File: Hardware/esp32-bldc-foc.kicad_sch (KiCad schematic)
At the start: 51 parts, among them J1 USB_C_Receptacle_USB2.0_14P, J2 Conn_01x03, J3 Conn_01x03, J4 Conn_01x02_Pin, J6 Conn_01x03, Q1 AP30H80Q, SW1 SW_Push_Dual, U1 ESP32-S3-WROOM-1, U2 SRV05-4, U3 MP1584EN-LF-P, U4 AMS1117, U5 EG2133, U6 INA181A1IDBVR

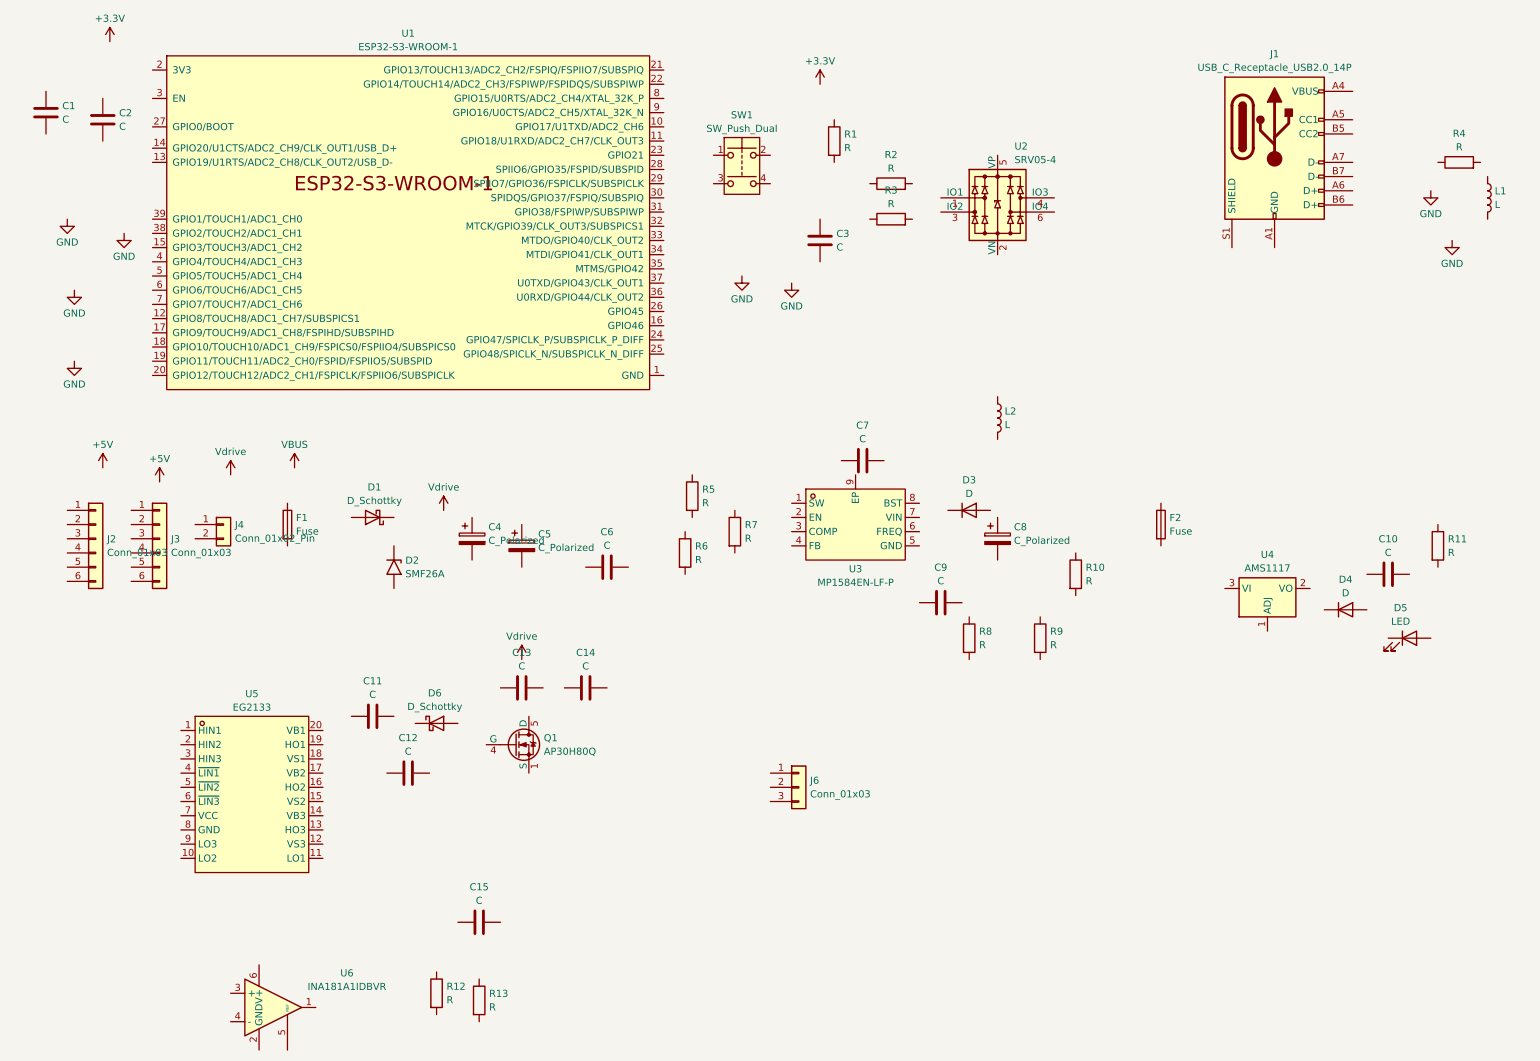
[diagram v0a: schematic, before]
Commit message: First cut of power regulation wiring
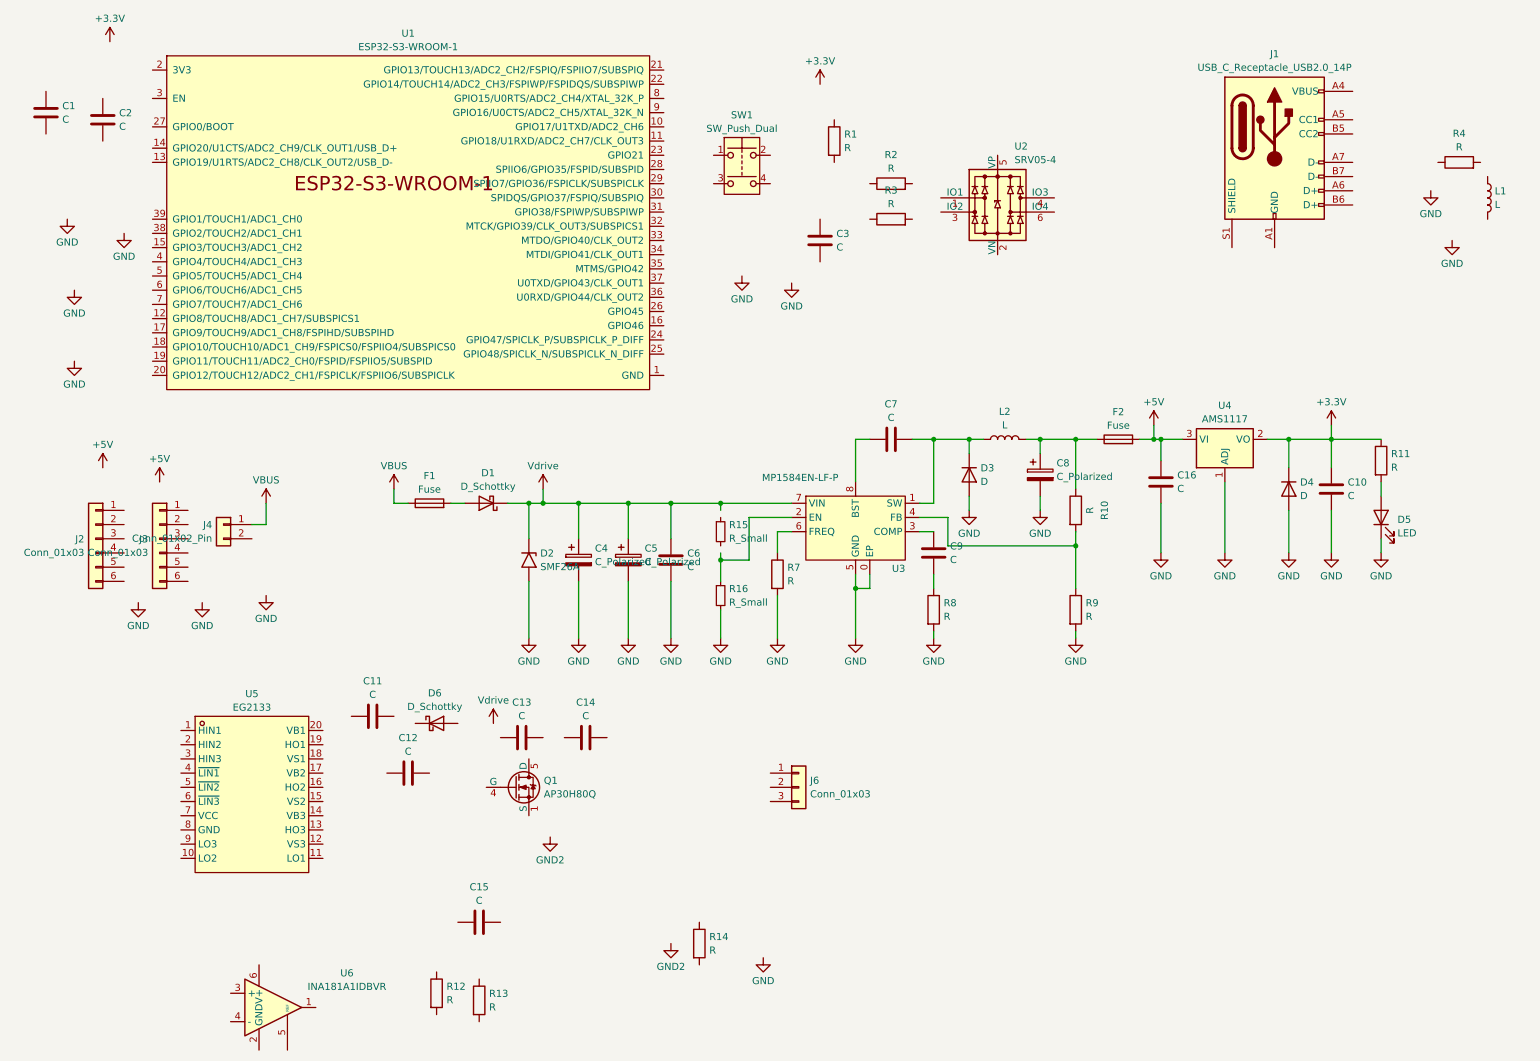
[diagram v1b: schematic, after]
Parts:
- removed R5, R6: R, symbol Device:R
- added C16: C, symbol Device:C
- added R14: R, symbol Device:R
- added R15, R16: R_Small, symbol Device:R_Small
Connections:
- net +3.3V: now also C10.2, D4.1 (K), R11.1, U4.2 (VO)
- net +5V: now also F2.2, U4.3 (VI), C16.2
- net GND: now also C10.1, C4.2, C5.2, C6.1, C8.2, D2.2 (A2), D3.2 (A), D4.2 (A), D5.1 (K), R7.2, R8.2, R9.2, U3.0 (EP), U3.5 (GND), U4.1 (ADJ), C16.1, R16.2
- net VBUS: now also F1.1, J4.1 (Pin_1)
- net Vdrive: now also C4.1, C5.1, C6.2, D1.1 (K), D2.1 (A1), U3.7 (VIN)
- net at R7.1: now also U3.6 (FREQ)
- net at R8.1: now also C9.1
- net at D1.2 (A): now also F1.2
- net at D5.2 (A): now also R11.2
- net at C8.1: now also F2.1, L2.2, R10.1
- net at C7.1: now also U3.8 (BST)
- net at C7.2: now also D3.1 (K), L2.1, U3.1 (SW)
- net at U3.2 (EN): now also R16.1
- net at U3.3 (COMP): now also C9.2
- net at U3.4 (FB): now also R10.2, R9.1
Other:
- moved on the sheet: C10, C13, C14, C4, C5, C6, C7, C8, C9, D1, D2, D3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

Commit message: Placed all components
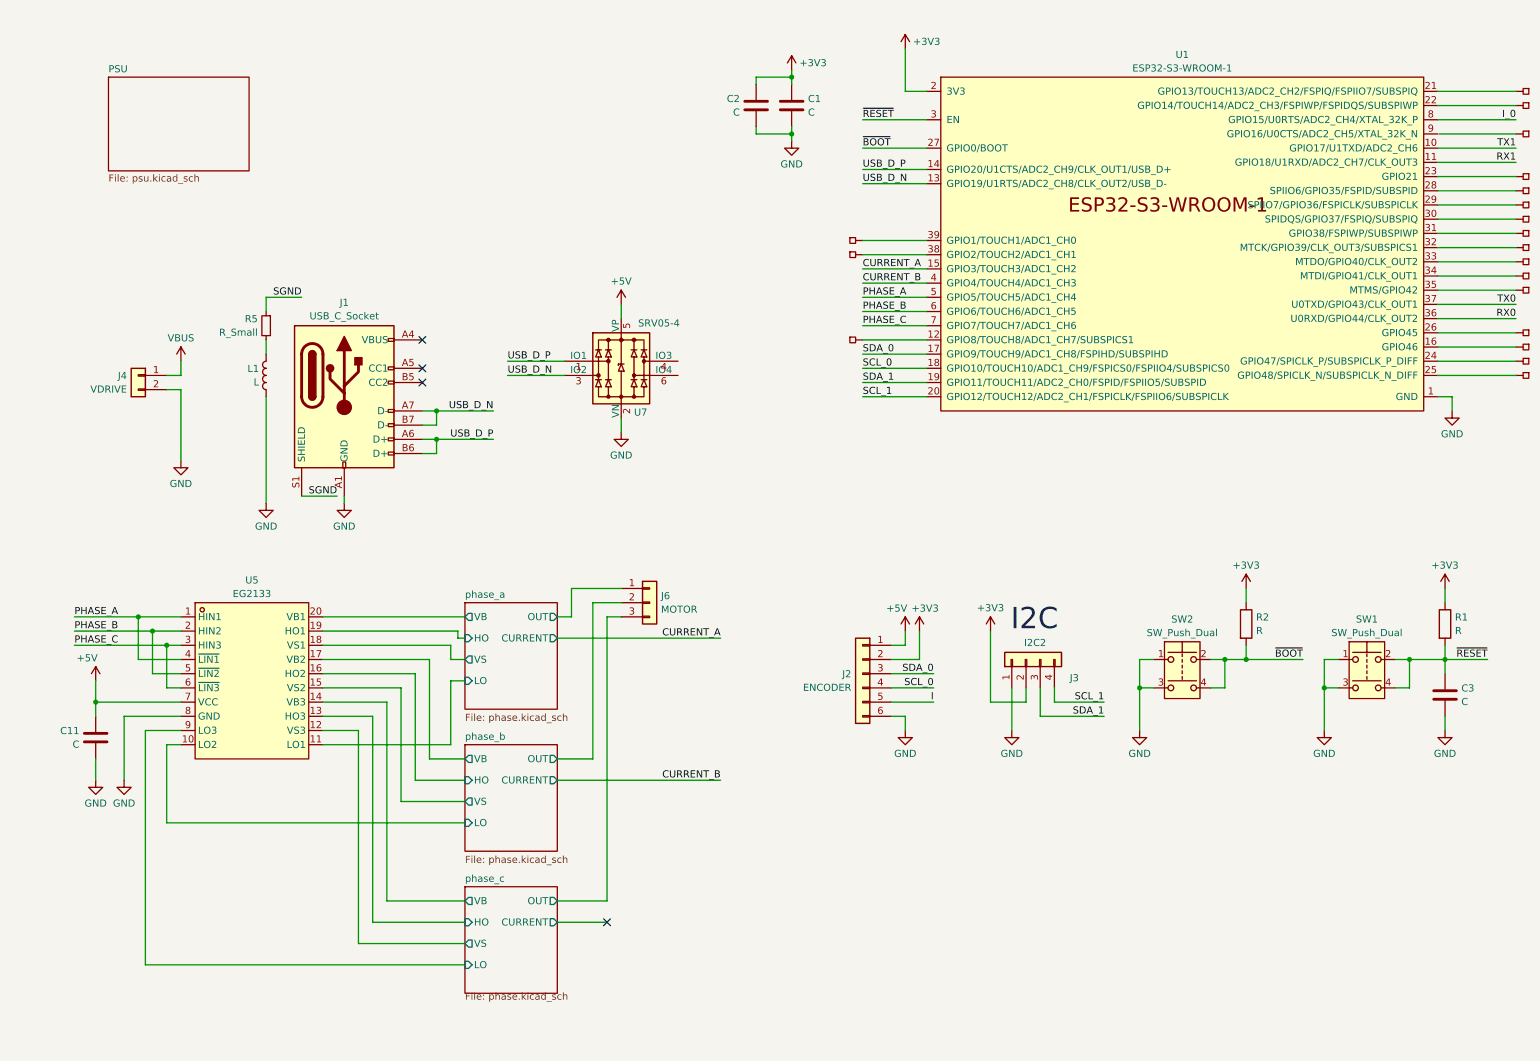
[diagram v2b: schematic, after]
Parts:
- removed C10, C12, C13, C14, C15, C16, C6, C7, C9: C, symbol Device:C
- removed C4, C5, C8: C_Polarized, symbol Device:C_Polarized
- removed D1, D6: D_Schottky, symbol Device:D_Schottky
- removed D2: SMF26A, Diode_SMD:D_SMF, symbol Diode:SMF26A
- removed D3, D4: D, symbol Device:D
- removed D5: LED, symbol Device:LED
- removed F1, F2: Fuse, symbol Device:Fuse
- removed J3: Conn_01x03, symbol Connector_Generic:Conn_01x06
- removed L2: L, symbol Device:L
- removed Q1: AP30H80Q, :DFN-8_L3.2-W3.1-P0.65-LS3.4-BL, symbol esp32-bldc-foc:AP30H80Q
- removed R10, R11, R12, R13, R14, R3, R4, R7, R8, R9: R, symbol Device:R
- removed R15, R16: R_Small, symbol Device:R_Small
- removed U2: SRV05-4, Package_TO_SOT_SMD:SOT-23-6, symbol afork-kicad-parts:SRV05-4
- removed U3: MP1584EN-LF-P, :SOIC-8_L4.9-W3.9-P1.27-LS6.0-TL-EP-1, symbol esp32-bldc-foc:MP1584EN-LF-P
- removed U4: AMS1117, Package_TO_SOT_SMD:SOT-223-3_TabPin2, symbol Regulator_Linear:AMS1117
- removed U6: INA181A1IDBVR, :SOT-23-6_L2.9-W1.6-P0.95-LS2.8-TL, symbol esp32-bldc-foc:INA181A1IDBVR
- added J3: I2C2, Connector_PinHeader_2.54mm:PinHeader_1x04_P2.54mm_Vertical, symbol Connector_Generic:Conn_01x04
- added JP1, JP10, JP11, JP12, JP13, JP14, JP15, JP16, JP17, JP18, JP19, JP2, JP3, JP4, JP5, JP6, JP7, JP8, JP9: PCB_Pin_Breakout, TestPoint:TestPoint_Pad_1.0x1.0mm, symbol afork-kicad-parts:PCB_Pin_Breakout
- added R5: R_Small, symbol Device:R_Small
- added SW2: SW_Push_Dual, symbol Switch:SW_Push_Dual
- added U7: SRV05-4, Package_TO_SOT_SMD:SOT-23-6, symbol afork-kicad-parts:SRV05-4
- J1: value USB_C_Receptacle_USB2.0_14P -> USB_C_Socket
- J2: value Conn_01x03 -> ENCODER
- J4: value Conn_01x02_Pin -> VDRIVE
- J6: value Conn_01x03 -> MOTOR
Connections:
- net +5V: now also C11.2, J2.1 (Pin_1), U5.7 (VCC), U7.5 (VP)
- net GND: now also C1.2, C11.1, C2.2, C3.2, J1.A1 (GND), J1.A12 (GND), J1.B1 (GND), J1.B12 (GND), J2.6 (Pin_6), J4.2 (Pin_2), L1.2, SW1.1, SW1.3, U1.1 (GND), U1.40 (GND), U1.41 (GND), U5.8 (GND), J3.1 (Pin_1), SW2.1, SW2.3, U7.2 (VN)
- net ~{RESET}: now reaches C3.1
- net ~{RESET}: now also R1.2, SW1.2, SW1.4, U1.3 (EN)
- net phase_a/OUT: now reaches J6.1 (Pin_1)
- net phase_b/OUT: now reaches J6.2 (Pin_2)
- net phase_c/OUT: now reaches J6.3 (Pin_3)
- net +3V3: now reaches J2.2 (Pin_2)
- net +3V3: now also C1.1, C2.1, R1.1, R2.1, U1.2 (3V3), J3.2 (Pin_2)
- net SDA_0: now reaches J2.3 (Pin_3)
- net SDA_0: now also U1.17 (GPIO9/TOUCH9/ADC1_CH8/FSPIHD/SUBSPIHD)
- net SCL_0: now reaches J2.4 (Pin_4)
- net SCL_0: now also U1.18 (GPIO10/TOUCH10/ADC1_CH9/FSPICS0/FSPIIO4/SUBSPICS0)
- net I: now reaches J2.5 (Pin_5)
- net PHASE_A: now reaches U5.1 (HIN1)
- net PHASE_A: now also U1.5 (GPIO5/TOUCH5/ADC1_CH4), U5.4 (~{LIN1})
- net phase_b/LO: now reaches U5.10 (LO2)
- net phase_a/LO: now reaches U5.11 (LO1)
- net phase_c/VS: now reaches U5.12 (VS3)
- net phase_c/HO: now reaches U5.13 (HO3)
- net phase_c/VB: now reaches U5.14 (VB3)
- net phase_b/VS: now reaches U5.15 (VS2)
- net phase_b/HO: now reaches U5.16 (HO2)
- net phase_b/VB: now reaches U5.17 (VB2)
- net phase_a/VS: now reaches U5.18 (VS1)
- net phase_a/HO: now reaches U5.19 (HO1)
- net PHASE_B: now reaches U5.2 (HIN2)
- net PHASE_B: now also U1.6 (GPIO6/TOUCH6/ADC1_CH5), U5.5 (~{LIN2})
- net phase_a/VB: now reaches U5.20 (VB1)
- net PHASE_C: now reaches U5.3 (HIN3)
- net PHASE_C: now also U1.7 (GPIO7/TOUCH7/ADC1_CH6), U5.6 (~{LIN3})
- net phase_c/LO: now reaches U5.9 (LO3)
- net at L1.1: now also R5.2
- net USB_D_P: now reaches J1.A6 (D+)
- net USB_D_P: now also J1.B6 (D+), U1.14 (GPIO20/U1CTS/ADC2_CH9/CLK_OUT1/USB_D+), U7.1 (IO1)
- net USB_D_N: now reaches J1.A7 (D-)
- net USB_D_N: now also J1.B7 (D-), U1.13 (GPIO19/U1RTS/ADC2_CH8/CLK_OUT2/USB_D-), U7.3 (IO2)
- net SGND: now reaches J1.S1 (SHIELD)
- net SGND: now also R5.1
- net ~{BOOT}: now reaches R2.2
- net ~{BOOT}: now also U1.27 (GPIO0/BOOT), SW2.2, SW2.4
- net TX1: now reaches U1.10 (GPIO17/U1TXD/ADC2_CH6)
- net RX1: now reaches U1.11 (GPIO18/U1RXD/ADC2_CH7/CLK_OUT3)
- net at U1.12 (GPIO8/TOUCH8/ADC1_CH7/SUBSPICS1): now also JP3.1
- net CURRENT_A: now reaches U1.15 (GPIO3/TOUCH3/ADC1_CH2)
- net at U1.16 (GPIO46): now also JP15.1
- net SDA_1: now reaches U1.19 (GPIO11/TOUCH11/ADC2_CH0/FSPID/FSPIIO5/SUBSPID)
- net SDA_1: now also J3.3 (Pin_3)
- net SCL_1: now reaches U1.20 (GPIO12/TOUCH12/ADC2_CH1/FSPICLK/FSPIIO6/SUBSPICLK)
- net SCL_1: now also J3.4 (Pin_4)
- net at U1.21 (GPIO13/TOUCH13/ADC2_CH2/FSPIQ/FSPIIO7/SUBSPIQ): now also JP19.1
- net at U1.22 (GPIO14/TOUCH14/ADC2_CH3/FSPIWP/FSPIDQS/SUBSPIWP): now also JP18.1
- net at U1.23 (GPIO21): now also JP5.1
- net at U1.24 (GPIO47/SPICLK_P/SUBSPICLK_P_DIFF): now also JP16.1
- net at U1.25 (GPIO48/SPICLK_N/SUBSPICLK_N_DIFF): now also JP17.1
- net at U1.26 (GPIO45): now also JP14.1
- net at U1.28 (SPIIO6/GPIO35/FSPID/SUBSPID): now also JP6.1
- net at U1.29 (SPIIO7/GPIO36/FSPICLK/SUBSPICLK): now also JP7.1
- net at U1.30 (SPIDQS/GPIO37/FSPIQ/SUBSPIQ): now also JP8.1
- net at U1.31 (GPIO38/FSPIWP/SUBSPIWP): now also JP9.1
- net at U1.32 (MTCK/GPIO39/CLK_OUT3/SUBSPICS1): now also JP10.1
- net at U1.33 (MTDO/GPIO40/CLK_OUT2): now also JP11.1
- net at U1.34 (MTDI/GPIO41/CLK_OUT1): now also JP12.1
- net at U1.35 (MTMS/GPIO42): now also JP13.1
- net RX0: now reaches U1.36 (U0RXD/GPIO44/CLK_OUT2)
- net TX0: now reaches U1.37 (U0TXD/GPIO43/CLK_OUT1)
- net at U1.38 (GPIO2/TOUCH2/ADC1_CH1): now also JP2.1
- net at U1.39 (GPIO1/TOUCH1/ADC1_CH0): now also JP1.1
- net CURRENT_B: now reaches U1.4 (GPIO4/TOUCH4/ADC1_CH3)
- net I_0: now reaches U1.8 (GPIO15/U0RTS/ADC2_CH4/XTAL_32K_P)
- no-connect marks 0 -> 4
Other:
- added sheet PSU (psu.kicad_sch)
- added sheet phase_a (phase.kicad_sch)
- added sheet phase_b (phase.kicad_sch)
- added sheet phase_c (phase.kicad_sch)
- note added: "I2C"
- moved on the sheet: C1, C11, C2, C3, J1, J2, J4, J6, L1, R1, SW1, U1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

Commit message: Reannotated
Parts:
- added P20, P21: PCB_Pin_Breakout, TestPoint:TestPoint_Pad_1.0x1.0mm, symbol afork-kicad-parts:PCB_Pin_Breakout
- renumbered SW1 to BOOT1, C2 to C1, C11 to C13, C1 to C2, J2 to J1, J3 to J2, J4 to J3, J6 to J4, JP1 to P1, JP8 to P10, JP9 to P11, JP10 to P12, JP11 to P13, JP12 to P14, JP13 to P15, JP14 to P16, JP15 to P17, JP16 to P18, JP17 to P19, JP2 to P2, JP3 to P3, JP19 to P4, JP18 to P5, JP4 to P6, JP5 to P7, JP6 to P8, JP7 to P9, R2 to R3, SW2 to RESET1, U7 to U3, U5 to U6, J1 to USB1
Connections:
- net ~{BOOT}: now also BOOT1.2, BOOT1.4, R1.2; no longer R3.2, RESET1.2, RESET1.4
- net ~{RESET}: now also R3.2, RESET1.2, RESET1.4; no longer BOOT1.2, BOOT1.4, R1.2
- net at U3.4 (IO3): now also P20.1
- net at U3.6 (IO4): now also P21.1
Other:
- moved on the sheet: C3

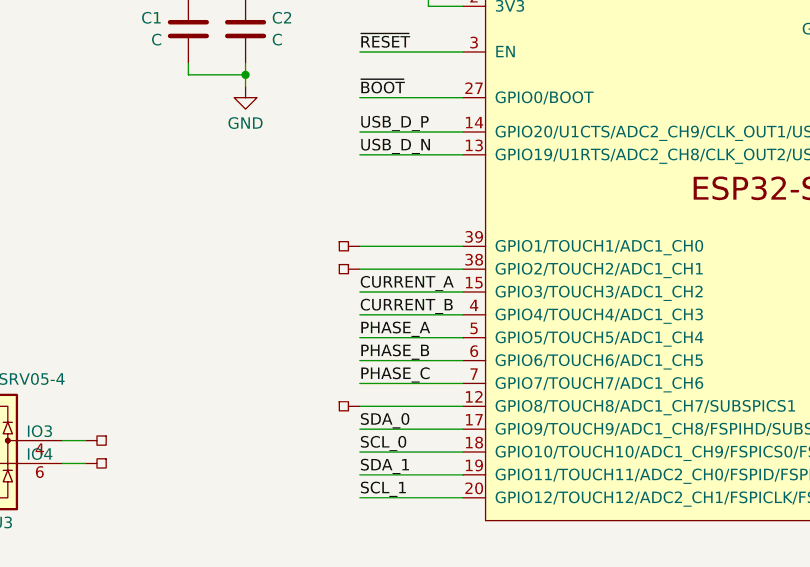
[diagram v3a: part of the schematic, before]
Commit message: Swapped some pins to allow for CURRENT3 if we need it.
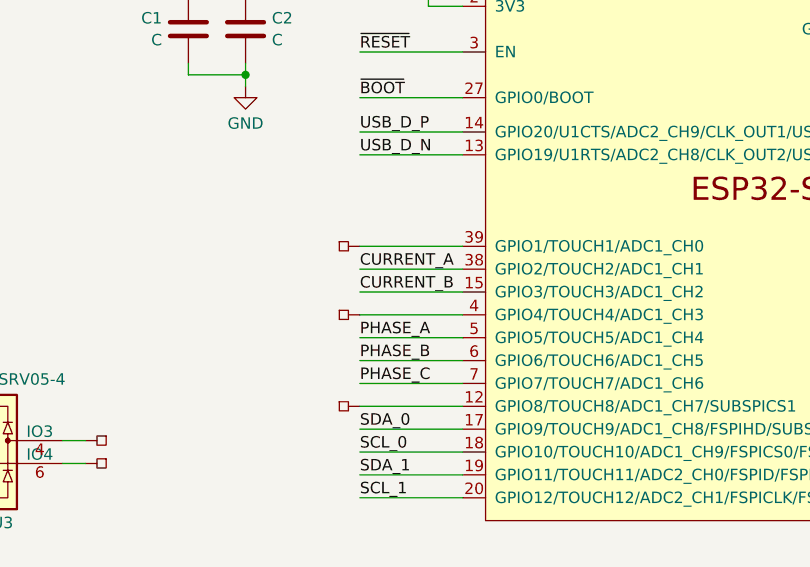
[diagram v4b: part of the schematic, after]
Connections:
- net CURRENT_A: now also U1.38 (GPIO2/TOUCH2/ADC1_CH1); no longer U1.15 (GPIO3/TOUCH3/ADC1_CH2)
- net CURRENT_B: now also U1.15 (GPIO3/TOUCH3/ADC1_CH2); no longer U1.4 (GPIO4/TOUCH4/ADC1_CH3)
- net at P2.1: now also U1.4 (GPIO4/TOUCH4/ADC1_CH3); no longer U1.38 (GPIO2/TOUCH2/ADC1_CH1)
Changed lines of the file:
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@@
 	(wire
 		(pts
-			(xy 161.29 63.5) (xy 172.72 63.5)
+			(xy 161.29 60.96) (xy 172.72 60.96)
 		)
 		(stroke
@@
 	(wire
 		(pts
-			(xy 161.29 58.42) (xy 172.72 58.42)
+			(xy 161.29 63.5) (xy 172.72 63.5)
 		)
 		(stroke
@@
 	(wire
 		(pts
-			(xy 161.29 60.96) (xy 172.72 60.96)
+			(xy 161.29 58.42) (xy 172.72 58.42)
 		)
 		(stroke
@@
 	)
 	(label "CURRENT_B"
-		(at 161.29 63.5 0)
+		(at 161.29 60.96 0)
 		(fields_autoplaced yes)
 		(effects
@@
 	)
 	(label "CURRENT_A"
-		(at 161.29 60.96 0)
+		(at 161.29 58.42 0)
 		(fields_autoplaced yes)
 		(effects
@@
 	(symbol
 		(lib_id "afork-kicad-parts:PCB_Pin_Breakout")
-		(at 158.75 58.42 0)
+		(at 158.75 63.5 0)
 		(mirror y)
 		(unit 1)
@@
 		(fields_autoplaced yes)
 		(property "Reference" "P2"
-			(at 158.75 56.388 0)
+			(at 158.75 61.468 0)
 			(effects
 				(font
@@
 		)
 		(property "Value" "PCB_Pin_Breakout"
-			(at 158.496 59.944 0)
+			(at 158.496 65.024 0)
 			(effects
 				(font
@@
 		)
 		(property "Footprint" "TestPoint:TestPoint_Pad_1.0x1.0mm"
-			(at 158.75 58.42 0)
+			(at 158.75 63.5 0)
 			(effects
 				(font
@@
 		)
 		(property "Datasheet" "~"
-			(at 158.75 58.42 0)
+			(at 158.75 63.5 0)
 			(effects
 				(font
@@
 		)
 		(property "Description" "PCB pin breakout"
-			(at 158.75 58.42 0)
+			(at 158.75 63.5 0)
 			(effects
 				(font
